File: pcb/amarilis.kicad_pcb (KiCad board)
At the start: 2 copper layers, 239.7 x 113 mm, 82 parts, among them SW1 SW_PUSH, SW10 SW_PUSH, SW11 SW_PUSH, SW12 SW_PUSH, SW13 SW_PUSH, SW14 SW_PUSH, SW15 SW_PUSH, SW16 SW_PUSH, SW17 SW_PUSH, SW18 SW_PUSH, SW19 SW_PUSH, SW2 SW_PUSH, SW20 SW_PUSH, SW21 SW_PUSH, SW22 SW_PUSH, SW23 SW_PUSH, SW24 SW_PUSH, SW25 SW_PUSH, SW26 SW_PUSH, SW27 SW_PUSH, SW28 SW_PUSH, SW29 SW_PUSH, SW3 SW_PUSH, SW30 SW_PUSH, SW31 SW_PUSH, SW32 SW_PUSH, SW33 SW_PUSH, SW34 SW_PUSH, SW35 SW_PUSH, SW36 SW_PUSH, SW4 SW_PUSH, SW5 SW_PUSH, SW6 SW_PUSH, SW7 SW_PUSH, SW8 SW_PUSH, SW9 SW_PUSH

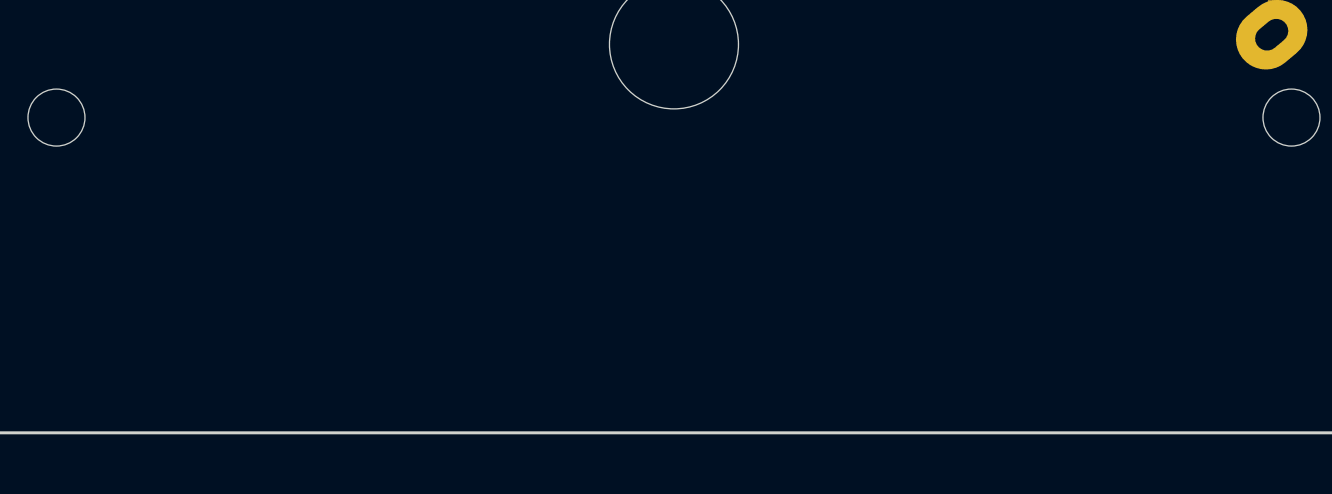
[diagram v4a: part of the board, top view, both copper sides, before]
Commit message: top and bottom plates
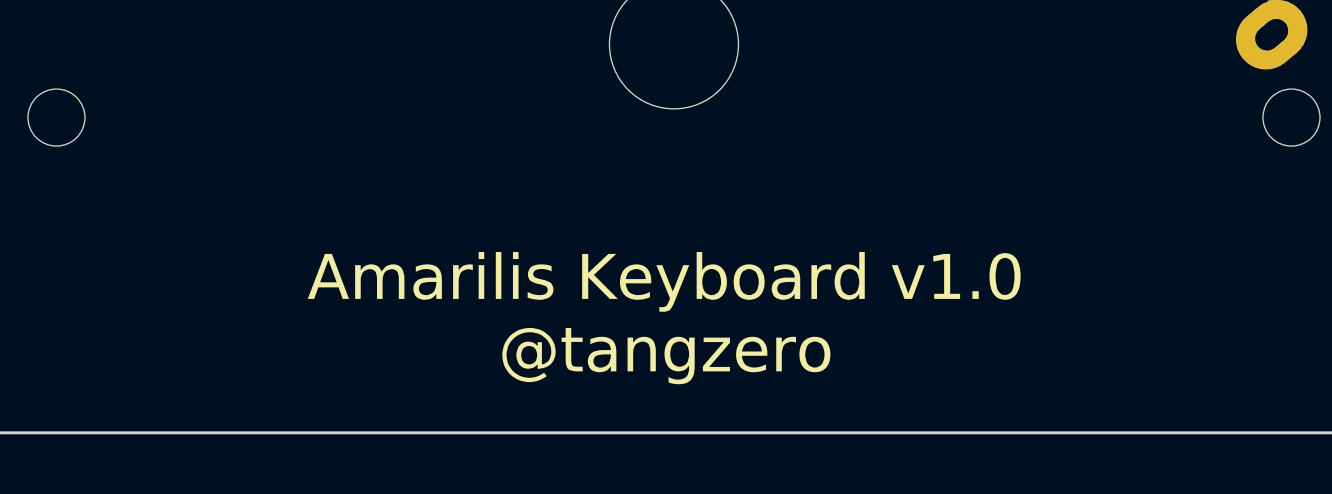
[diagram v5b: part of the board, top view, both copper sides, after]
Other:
- board text added: "Amarilis Keyboard v1.0 @tangzero"
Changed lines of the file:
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@@
   (gr_arc (start 39.2 47.8) (mid 41.456213 44.962788) (end 45 44.2) (layer "Edge.Cuts") (width 0.1))
   (gr_arc (start 251.05 44.2) (mid 254.593787 44.962788) (end 256.85 47.8) (layer "Edge.Cuts") (width 0.1))
+  (gr_text "Amarilis Keyboard v1.0\n@tangzero" (at 147.75 153.25) (layer "F.SilkS")
+    (effects (font (size 1.5 1.5) (thickness 0.3)))
+  )
   (segment (start 130.6 94.559188) (end 132.459188 92.7) (width 0.25) (layer "F.Cu") (net 1))
   (segment (start 150.115 92.7) (end 150.565 92.25) (width 0.25) (layer "F.Cu") (net 1))
